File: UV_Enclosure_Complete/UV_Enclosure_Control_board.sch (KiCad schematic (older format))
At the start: 52 parts

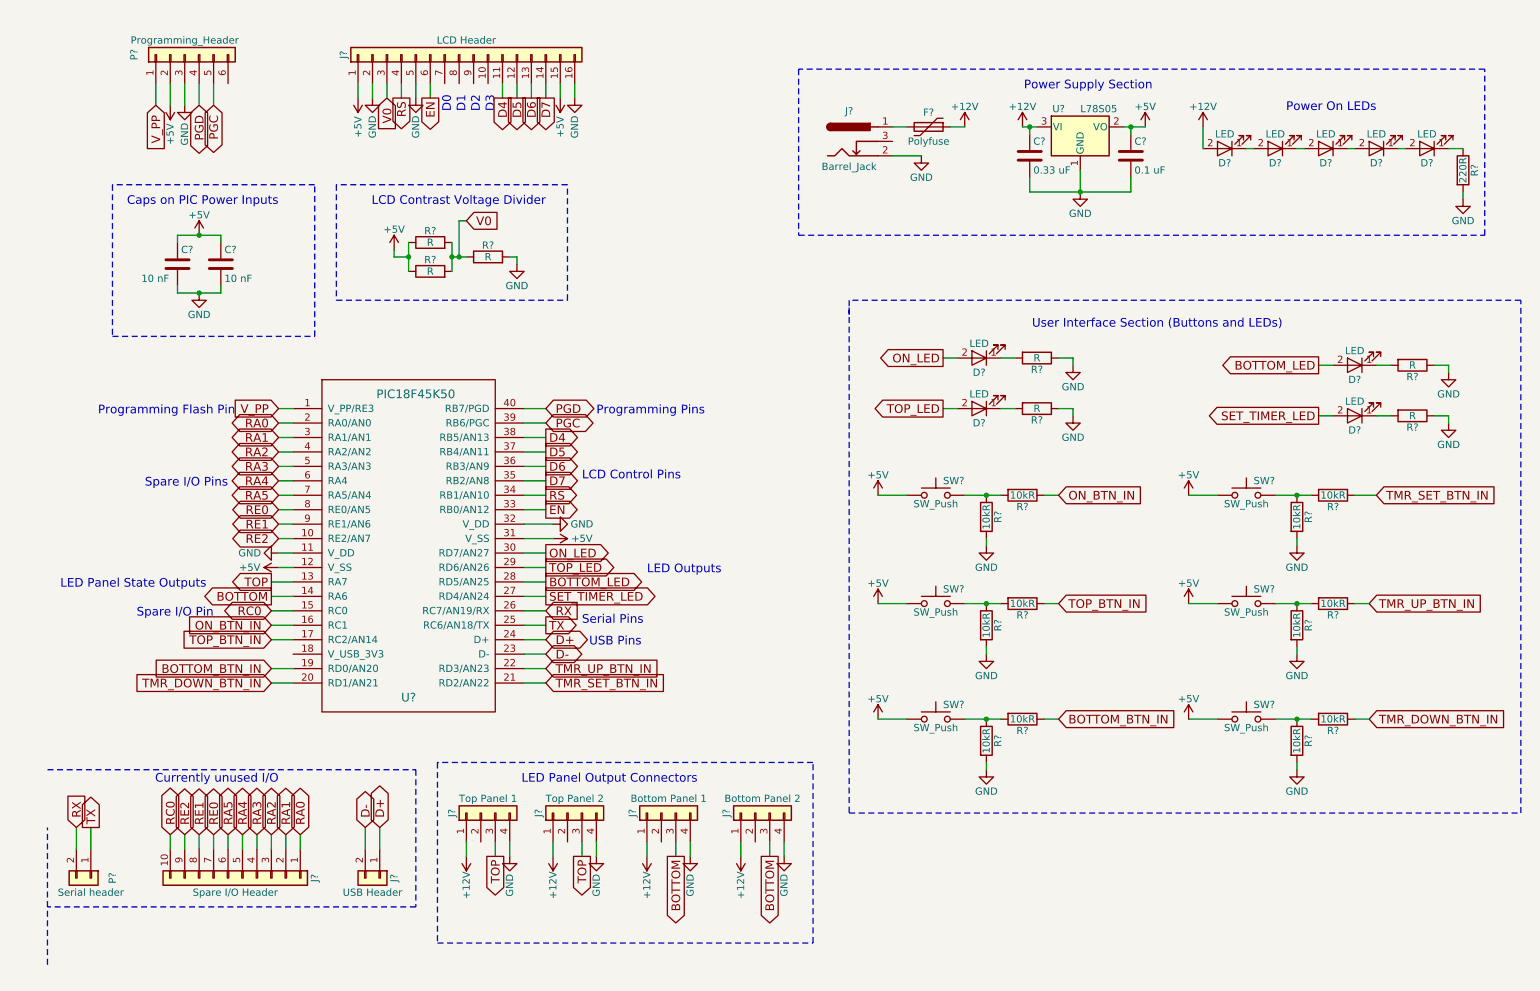
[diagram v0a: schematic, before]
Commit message: Changed LCD header to an LCD component.
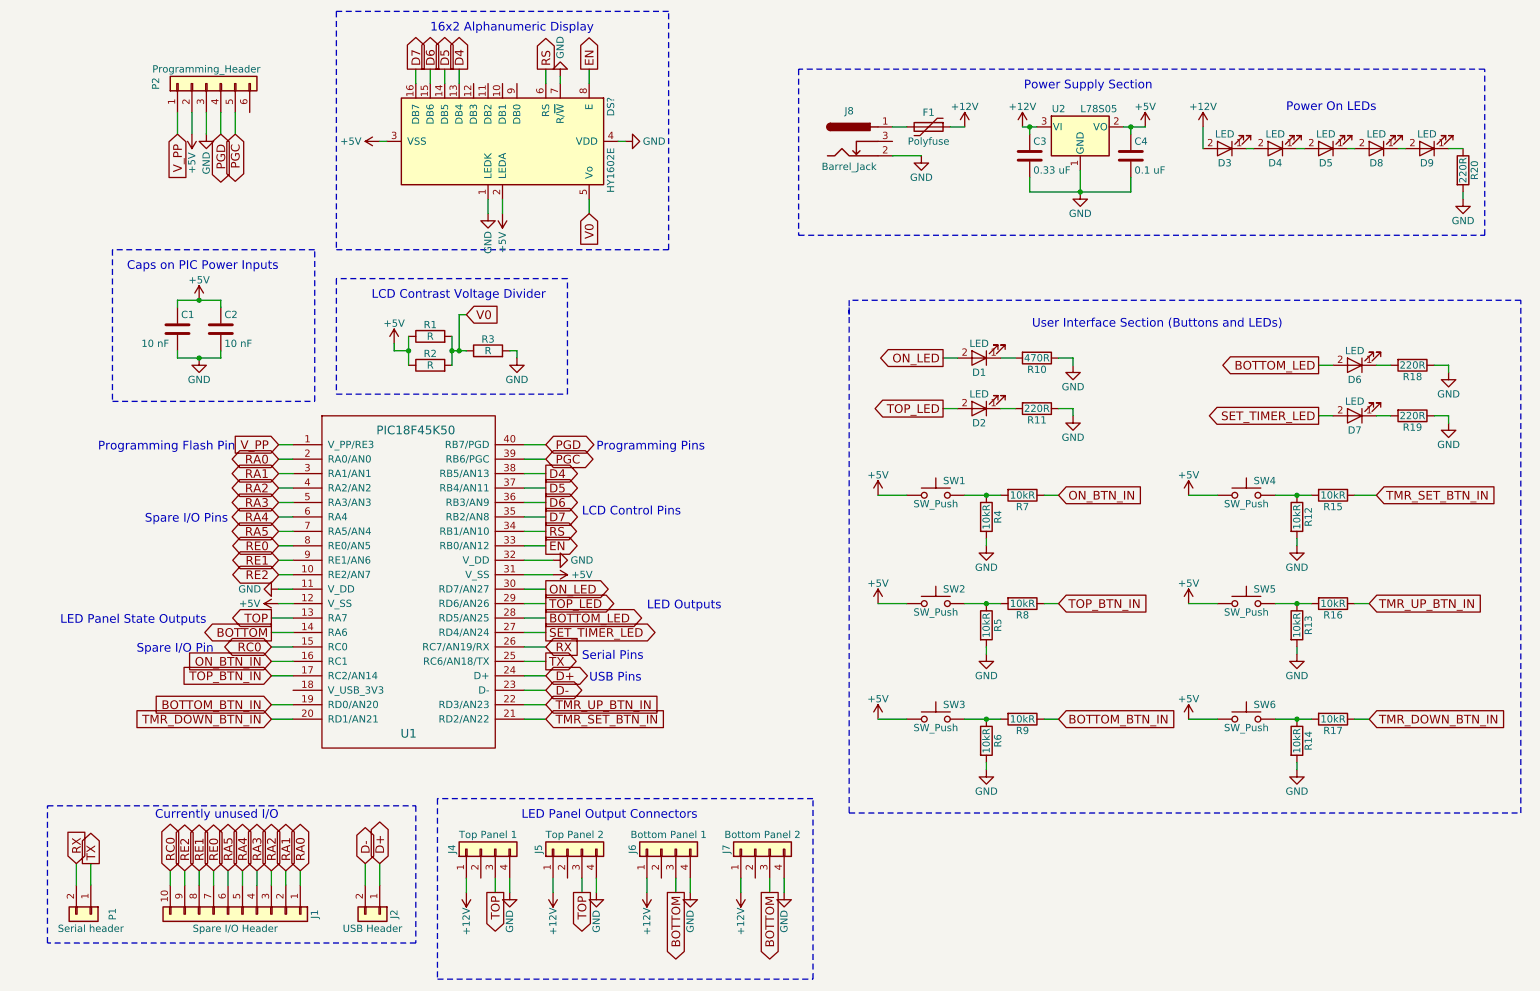
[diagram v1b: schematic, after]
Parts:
- removed J?: LCD Header, symbol Conn_01x16
- added DS?: HY1602E, Displays:HY1602E, symbol HY1602E
- C1, C2: renamed from C?; footprint (none) -> Capacitors_THT:C_Disc_D3.0mm_W2.0mm_P2.50mm
- C3: renamed from C?; footprint (none) -> Capacitors_THT:C_Rect_L9.0mm_W4.9mm_P7.50mm_MKT
- C4: renamed from C?; footprint (none) -> Capacitors_THT:C_Rect_L9.0mm_W3.2mm_P7.50mm_MKT
- D1, D2, D3, D4, D5, D6, D7, D8, D9: renamed from D?; footprint (none) -> LEDs:LED_D5.0mm
- J1: renamed from J?; footprint (none) -> Pin_Headers:Pin_Header_Straight_1x10_Pitch2.54mm
- J2: renamed from J?; footprint (none) -> Pin_Headers:Pin_Header_Straight_1x02_Pitch2.54mm
- J4, J5, J6, J7: renamed from J?; footprint (none) -> Pin_Headers:Pin_Header_Straight_1x04_Pitch2.54mm
- J8: renamed from J?; footprint (none) -> Connectors:BARREL_JACK
- P1: renamed from P?; footprint (none) -> Pin_Headers:Pin_Header_Straight_1x02_Pitch2.54mm
- P2: renamed from P?; footprint (none) -> Pin_Headers:Pin_Header_Straight_1x06_Pitch2.54mm
- R1, R12, R13, R14, R15, R16, R17, R2, R20, R3, R4, R5, R6, R7, R8, R9: renamed from R?; footprint (none) -> Resistors_THT:R_Axial_DIN0309_L9.0mm_D3.2mm_P12.70mm_Horizontal
- R10: renamed from R?; value R -> 470R; footprint (none) -> Resistors_THT:R_Axial_DIN0309_L9.0mm_D3.2mm_P12.70mm_Horizontal
- R11, R18, R19: renamed from R?; value R -> 220R; footprint (none) -> Resistors_THT:R_Axial_DIN0309_L9.0mm_D3.2mm_P12.70mm_Horizontal
- SW1, SW2, SW3, SW4, SW5, SW6: renamed from SW?; footprint (none) -> Buttons_Switches_THT:SW_Tactile_Straight_KSA0Axx1LFTR
- U2: renamed from U?; footprint (none) -> TO_SOT_Packages_THT:TO-220-3_Horizontal
- gave numbers to parts that had none: 2
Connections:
- net +5V: now also DS?.2 (LEDA), DS?.3 (VSS)
- net D4: now also DS?.13 (DB4)
- net D5: now also DS?.14 (DB5)
- net D6: now also DS?.15 (DB6)
- net D7: now also DS?.16 (DB7)
- net EN: now also DS?.8 (E)
- net GND: now also DS?.1 (LEDK), DS?.4 (VDD), DS?.7 (R/~W)
- net RS: now also DS?.6 (RS)
- net V0: now also DS?.5 (Vo)
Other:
- note added: "16x2 Alphanumeric Display"
- note removed: "D0"
- note removed: "D1"
- note removed: "D2"
- note removed: "D3"
- moved on the sheet: C1, C2, J1, J2, J4, J5, J6, J7, P1, P2, R1, R2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

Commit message: Added 5V header just in case any future additions require it.
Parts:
- removed DS?: HY1602E, Displays:HY1602E, symbol HY1602E
- added DS1: WC1602A, Displays:WC1602A, symbol WC1602A
- added J3: 5V Header, Pin_Headers:Pin_Header_Straight_1x02_Pitch2.54mm, symbol Conn_01x02
- F1: footprint (none) -> Fuses:Polyfuse-2A-Square-Horizontal
- U1: footprint (none) -> DIP:DIP-40_0
- U2: symbol L78S05 -> L78S05-RESCUE-UV_Enclosure_Control_board-RESCUE-UV_Enclosure_Control_board
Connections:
- net +12V: now also U2.1 (VI); no longer U2.3 (VI)
- net +5V: now also U2.3 (VO), DS1.1 (VSS), DS1.15 (LED(+)), J3.1 (Pin_1); no longer U2.2 (VO)
- net D4: now also DS1.11 (D4)
- net D5: now also DS1.12 (D5)
- net D6: now also DS1.13 (D6)
- net D7: now also DS1.14 (D7)
- net EN: now also DS1.6 (E)
- net GND: now also U2.2 (GND), DS1.16 (LED(-)), DS1.2 (VDD), DS1.5 (R/W), J3.2 (Pin_2); no longer U2.1 (GND)
- net RS: now also DS1.4 (RS)
- net V0: now also DS1.3 (VO)
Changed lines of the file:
@@
 EESchema Schematic File Version 2
+LIBS:UV_Enclosure_Control_board-rescue
 LIBS:power
 LIBS:device
@@
 LIBS:contrib
 LIBS:valves
-LIBS:PIC
 LIBS:Regulators-local
 LIBS:UV_Enclosure_Control_board-cache
@@
 F 0 "U1" H 3200 3500 60  0000 C CNN
 F 1 "PIC18F45K50" H 3250 5600 60  0000 C CNN
-F 2 "" H 3200 4550 60  0001 C CNN
+F 2 "DIP:DIP-40_0" H 3200 4550 60  0001 C CNN
 F 3 "" H 3200 4550 60  0001 C CNN
 	1    3200 4550
@@
 Text GLabel 4450 2000 3    60   Input ~ 0
 V0
-Text GLabel 4150 1000 1    60   Output ~ 0
+Text GLabel 4250 1000 1    60   Output ~ 0
 RS
 $Comp
 L GND #PWR011
 U 1 1 5A075638
-P 4250 1050
-F 0 "#PWR011" H 4250 800 50  0001 C CNN
-F 1 "GND" V 4250 850 50  0000 C CNN
-F 2 "" H 4250 1050 50  0001 C CNN
-F 3 "" H 4250 1050 50  0001 C CNN
-	1    4250 1050
+P 4350 1050
+F 0 "#PWR011" H 4350 800 50  0001 C CNN
+F 1 "GND" V 4350 850 50  0000 C CNN
+F 2 "" H 4350 1050 50  0001 C CNN
+F 3 "" H 4350 1050 50  0001 C CNN
+	1    4350 1050
 	-1   0    0    1
 $EndComp
@@
 L +5V #PWR012
 U 1 1 5A075904
-P 3850 2000
-F 0 "#PWR012" H 3850 1850 50  0001 C CNN
-F 1 "+5V" V 3850 2200 50  0000 C CNN
-F 2 "" H 3850 2000 50  0001 C CNN
-F 3 "" H 3850 2000 50  0001 C CNN
-	1    3850 2000
+P 4150 2000
+F 0 "#PWR012" H 4150 1850 50  0001 C CNN
+F 1 "+5V" V 4150 2200 50  0000 C CNN
+F 2 "" H 4150 2000 50  0001 C CNN
+F 3 "" H 4150 2000 50  0001 C CNN
+	1    4150 2000
 	-1   0    0    1
 $EndComp
@@
 L GND #PWR013
 U 1 1 5A075933
-P 3750 2000
-F 0 "#PWR013" H 3750 1750 50  0001 C CNN
-F 1 "GND" V 3750 1800 50  0000 C CNN
-F 2 "" H 3750 2000 50  0001 C CNN
-F 3 "" H 3750 2000 50  0001 C CNN
-	1    3750 2000
+P 4050 2000
+F 0 "#PWR013" H 4050 1750 50  0001 C CNN
+F 1 "GND" V 4050 1800 50  0000 C CNN
+F 2 "" H 4050 2000 50  0001 C CNN
+F 3 "" H 4050 2000 50  0001 C CNN
+	1    4050 2000
 	1    0    0    -1
 $EndComp
@@
 	4450 2000 4450 1900
 Wire Wire Line
-	4150 1000 4150 1100
+	4250 1000 4250 1100
 Wire Wire Line
 	4450 1000 4450 1100
@@
 	3250 1000 3250 1100
 Wire Wire Line
-	3850 2000 3850 1900
-Wire Wire Line
-	3750 2000 3750 1900
+	4150 2000 4150 1900
+Wire Wire Line
+	4050 2000 4050 1900
 Text GLabel 5050 6700 3    60   Output ~ 0
 BOTTOM
@@
 F 0 "F1" V 6700 1400 50  0000 C CNN
 F 1 "Polyfuse" V 6900 1400 50  0000 C CNN
-F 2 "" H 6850 1200 50  0001 L CNN
+F 2 "Fuses:Polyfuse-2A-Square-Horizontal" H 6850 1200 50  0001 L CNN
 F 3 "" H 6800 1400 50  0001 C CNN
 	1    6800 1400
@@
 	6550 1400 6650 1400
 $Comp
-L L78S05 U2
+L L78S05-RESCUE-UV_Enclosure_Control_board-RESCUE-UV_Enclosure_Control_board U2
 U 1 1 5A0788C7
 P 7850 1400
@@
 Wire Notes Line
 	1150 2250 1150 3300
-$Comp
-L HY1602E DS?
-U 1 1 5A0759BD
-P 3850 1500
-F 0 "DS?" H 3610 2250 50  0000 C CNN
-F 1 "HY1602E" H 4050 2250 50  0000 C CNN
-F 2 "Displays:HY1602E" H 3850 600 50  0001 C CIN
-F 3 "" H 4050 1600 50  0001 C CNN
-	1    3850 1500
-	0    1    1    0
-$EndComp
 Wire Notes Line
 	6000 7300 6000 6050
@@
 16x2 Alphanumeric Display
 Wire Wire Line
-	4250 1050 4250 1100
-Wire Wire Line
 	3050 1500 3000 1500
 Wire Wire Line
 	4700 1500 4650 1500
 Wire Notes Line
-	2700 600  2700 2250
-Wire Notes Line
-	2700 2250 5000 2250
-Wire Notes Line
-	5000 2250 5000 600
+	5000 600  5000 2300
 Wire Notes Line
 	5000 600  2700 600
 Wire Notes Line
 	700  7050 700  6100
+$Comp
+L WC1602A DS1
+U 1 1 5A074A06
+P 3850 1500
+F 0 "DS1" H 3620 2250 50  0000 C CNN
+F 1 "WC1602A" H 4060 2250 50  0000 C CNN
+F 2 "Displays:WC1602A" H 3850 600 50  0001 C CIN
+F 3 "" H 4550 1500 50  0001 C CNN
+	1    3850 1500
+	0    1    1    0
+$EndComp
+Wire Wire Line
+	4350 1050 4350 1100
+Wire Notes Line
+	5000 2300 2700 2300
+Wire Notes Line
+	2700 2300 2700 600
+$Comp
+L +5V #PWR047
+U 1 1 5A075B66
+P 750 1150
+F 0 "#PWR047" H 750 1000 50  0001 C CNN
+F 1 "+5V" H 750 1290 50  0000 C CNN
+F 2 "" H 750 1150 50  0001 C CNN
+F 3 "" H 750 1150 50  0001 C CNN
+	1    750  1150
+	1    0    0    -1
+$EndComp
+$Comp
+L GND #PWR048
+U 1 1 5A075C4A
+P 750 1450
+F 0 "#PWR048" H 750 1200 50  0001 C CNN
+F 1 "GND" H 750 1300 50  0000 C CNN
+F 2 "" H 750 1450 50  0001 C CNN
+F 3 "" H 750 1450 50  0001 C CNN
+	1    750  1450
+	1    0    0    -1
+$EndComp
+$Comp
+L Conn_01x02 J3
+U 1 1 5A075D2E
+P 1050 1250
+F 0 "J3" H 1050 1350 50  0000 C CNN
+F 1 "5V Header" H 1050 1050 50  0000 C CNN
+F 2 "Pin_Headers:Pin_Header_Straight_1x02_Pitch2.54mm" H 1050 1250 50  0001 C CNN
+F 3 "" H 1050 1250 50  0001 C CNN
+	1    1050 1250
+	1    0    0    -1
+$EndComp
+Wire Wire Line
+	750  1150 750  1250
+Wire Wire Line
+	750  1250 850  1250
+Wire Wire Line
+	750  1450 750  1350
+Wire Wire Line
+	750  1350 850  1350
 $EndSCHEMATC

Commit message: Added pull up resistor on V_PP and started routing traces.
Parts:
- added R21: 10kR, Resistors_THT:R_Axial_DIN0309_L9.0mm_D3.2mm_P12.70mm_Horizontal, symbol R
- R1: value R -> 100kR
- R2: value R -> 10kR
- R3: value R -> 1kR
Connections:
- net +5V: now also R21.1
- net V_PP: now also R21.2
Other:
- moved on the sheet: C1, C2
